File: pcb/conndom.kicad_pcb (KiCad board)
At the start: 2 copper layers, 0 parts

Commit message: first pcb design
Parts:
- added C1: 104, Capacitor_SMD:C_0805_2012Metric, F.Cu at (180.6, 92.7)
- added D1: SK6812, LED_SMD:LED_SK6812_PLCC4_5.0x5.0mm_P3.2mm, F.Cu at (183.4, 87.5)
- added J1: 5V, rpi-zero-2-w-testpads:2mm-testpad-conn-plated, F.Cu at (155.8, 103.7)
- added J10: USB A WIFI, UJ2-AH-4-TH:CUI_UJ2-AH-4-TH, F.Cu at (170.4, 105.4)
- added J2: GND, rpi-zero-2-w-testpads:2mm-testpad-conn-plated, F.Cu at (156.1, 106.3)
- added J3: USB_DP, rpi-zero-2-w-testpads:1.7mm-testpad-conn-plated, F.Cu at (142.3, 108.1)
- added J4: USB_DM, rpi-zero-2-w-testpads:1.7mm-testpad-conn-plated, F.Cu at (144.4, 108.1)
- added J5: 3V3, rpi-zero-2-w-testpads:2mm-testpad-conn-plated, F.Cu at (118.5, 87.5)
- added J6: GND, rpi-zero-2-w-testpads:2mm-testpad-conn-plated, F.Cu at (158.7, 84.8)
- added J7: PWR, rpi-zero-2-w-testpads:1.7mm-testpad-conn-plated, F.Cu at (158.7, 82.2)
- added J8: LED, rpi-zero-2-w-testpads:1.7mm-testpad-conn-plated, F.Cu at (156.1, 82.2)
- added J9: USB C PWR, UJC-HP2-3-SMT-TR:CUI_UJC-HP2-3-SMT-TR, F.Cu at (196.3, 87.4)
- added R1: 10k, Resistor_SMD:R_0805_2012Metric, F.Cu at (172.8, 93.0)
- added R2: 500, Resistor_SMD:R_0805_2012Metric, F.Cu at (178.6, 84.1)
- added R3: 5K1, Resistor_SMD:R_0805_2012Metric, F.Cu at (188.9, 82.9)
- added R4: 5K1, Resistor_SMD:R_0805_2012Metric, F.Cu at (187.8, 89.0)
- added REF**: zero-2-w-testpads, rpi-zero-2-w-testpads:rpi-zero-2-w-testpads, F.Cu at (167.0, 110.0)
- added S1: PWR, TS02-66-55-BK-260-LCR-D:SW_TS02-66-55-BK-260-LCR-D, F.Cu at (172.8, 87.4)
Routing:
- net GND: track 0.00 -> 123.7 mm, vias 0 -> 2
- net Net-(D1-VDD): track 0.00 -> 76.7 mm
- net +5V: track 0.00 -> 54.2 mm, vias 0 -> 2
- net Net-(J3-Pin_1): track 0.00 -> 31.1 mm
- net Net-(J4-Pin_1): track 0.00 -> 29.1 mm
- net Net-(J7-Pin_1): track 0.00 -> 27.4 mm, vias 0 -> 1
- net Net-(J8-Pin_1): track 0.00 -> 24.2 mm, vias 0 -> 1
- net Net-(J9-CC2): track 0.00 -> 6.05 mm
- net Net-(J9-CC1): track 0.00 -> 4.48 mm
- net Net-(D1-DIN): track 0.00 -> 3.26 mm
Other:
- board outline added: 82 x 32 mm

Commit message: fix missplaced pads for usb dp, dm
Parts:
- moved J3 2.15 mm to (144.4, 108.1)
- moved J4 2.15 mm to (142.3, 108.1)
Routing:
- net Net-(J4-Pin_1): track 29.1 -> 31.9 mm, vias 0 -> 1
- net Net-(J3-Pin_1): track 31.1 -> 29.0 mm
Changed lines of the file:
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@@
 	(footprint "rpi-zero-2-w-testpads:1.7mm-testpad-conn-plated"
 		(layer "F.Cu")
-		(at 142.3 108.1)
+		(at 144.45 108.1)
 		(property "Reference" "J3"
 			(at -15 6 0)
@@
 	(footprint "rpi-zero-2-w-testpads:1.7mm-testpad-conn-plated"
 		(layer "F.Cu")
-		(at 144.45 108.1)
+		(at 142.3 108.1)
 		(property "Reference" "J4"
 			(at -15 6 0)
@@
 	)
 	(segment
-		(start 149.5 100.9)
-		(end 142.3 108.1)
+		(start 150.75 101.8)
+		(end 168.7 101.8)
 		(width 0.5)
 		(layer "B.Cu")
@@
 	)
 	(segment
-		(start 170.43 100.9)
-		(end 149.5 100.9)
+		(start 144.45 108.1)
+		(end 150.75 101.8)
 		(width 0.5)
 		(layer "B.Cu")
@@
 	)
 	(segment
-		(start 166.9 102.9)
-		(end 165.75 101.75)
+		(start 169.6 100.9)
+		(end 170.43 100.9)
 		(width 0.5)
 		(layer "B.Cu")
-		(net 7)
+		(net 6)
 	)
 	(segment
-		(start 150.8 101.75)
-		(end 144.45 108.1)
+		(start 168.7 101.8)
+		(end 169.6 100.9)
 		(width 0.5)
 		(layer "B.Cu")
+		(net 6)
+	)
+	(segment
+		(start 169.7 102.9)
+		(end 170.43 102.9)
+		(width 0.5)
+		(layer "F.Cu")
+		(net 7)
+	)
+	(segment
+		(start 167.8 101)
+		(end 169.7 102.9)
+		(width 0.5)
+		(layer "F.Cu")
+		(net 7)
+	)
+	(via
+		(at 167.8 101)
+		(size 0.7)
+		(drill 0.3)
+		(layers "F.Cu" "B.Cu")
+		(free yes)
 		(net 7)
 	)
 	(segment
-		(start 170.43 102.9)
-		(end 166.9 102.9)
+		(start 149.4 101)
+		(end 167.8 101)
 		(width 0.5)
 		(layer "B.Cu")
@@
 	)
 	(segment
-		(start 165.75 101.75)
-		(end 150.8 101.75)
+		(start 142.3 108.1)
+		(end 149.4 101)
 		(width 0.5)
 		(layer "B.Cu")

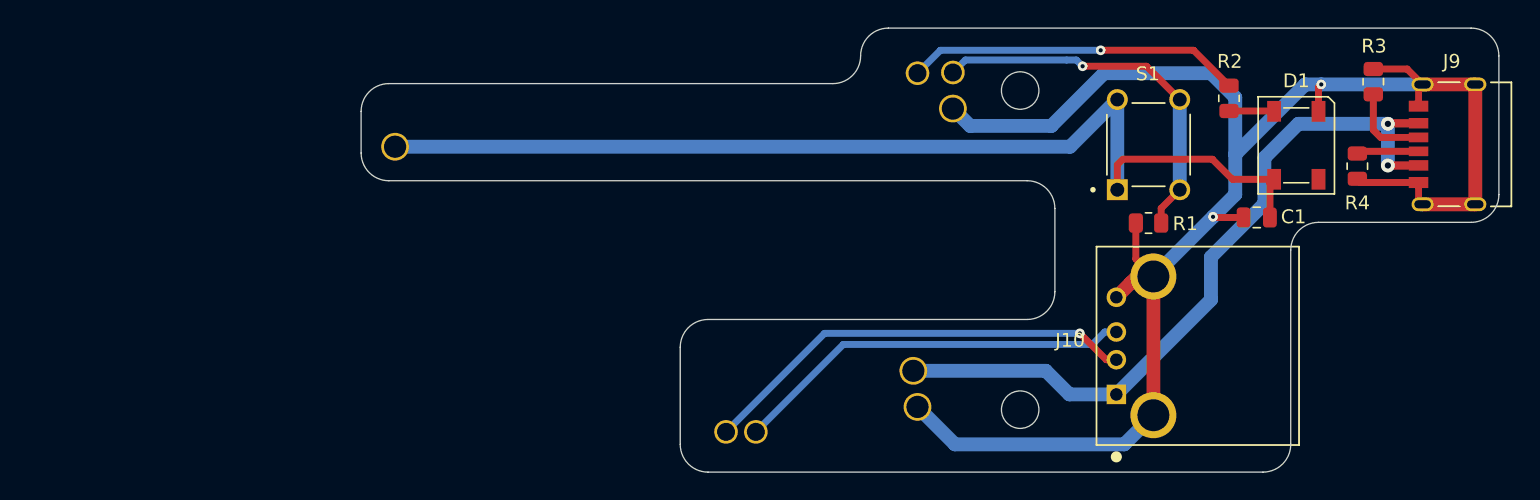
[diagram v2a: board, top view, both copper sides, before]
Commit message: update footprints, renaming
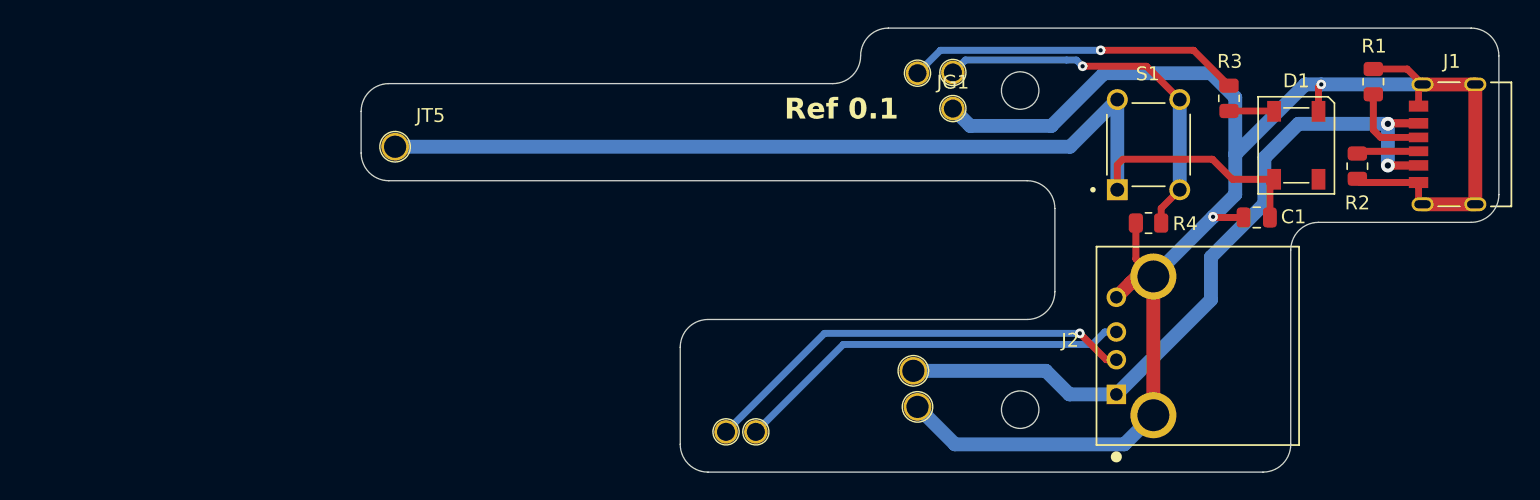
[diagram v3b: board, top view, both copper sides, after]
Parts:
- JG1: renamed from J6; footprint rpi-zero-2-w-testpads:2mm-testpad-conn-plated -> rpi-zero-2-w-testpads:1.7mm-testpad-conn-plated
- JG2: renamed from J7; value PWR -> GPIO21
- JG3: renamed from J8; value LED -> GPIO12
- renumbered J9 to J1, J10 to J2, J1 to JT1, J2 to JT2, J3 to JT3, J4 to JT4, J5 to JT5, R3 to R1, R4 to R2, R2 to R3, R1 to R4
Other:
- board text added: "Ref 0.1"

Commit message: pcb rev 0.2
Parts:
- moved JG3 17.6 mm to (138.5, 82.2)
- moved R4 16.2 mm to (161.3, 81.5), turned to 180 degrees
- moved R1 12.3 mm to (176.9, 85.1)
- moved R3 12.2 mm to (166.8, 87.0)
- moved J1 12.1 mm to (184.2, 87.0)
- moved D1 11.7 mm to (171.7, 87.0)
- moved S1 11.4 mm to (161.3, 87.0), turned to -90 degrees
- moved R2 10.9 mm to (176.9, 88.9)
- moved J2 10.9 mm to (159.6, 104.3)
- moved JG1 10.0 mm to (148.6, 84.8)
- moved JG2 10.0 mm to (148.6, 82.2)
- moved JT1 10.0 mm to (145.8, 103.7)
- moved JT3 10.0 mm to (134.4, 108.1)
- moved JT2 10.0 mm to (146.1, 106.3)
- moved JT5 10.0 mm to (108.5, 87.6)
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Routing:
- net GND: track 123.7 -> 108.9 mm
- net Net-(JG3-Pin_1): track 24.2 -> 34.0 mm
- net Net-(JG2-Pin_1): track 27.4 -> 21.2 mm, vias 1 -> 0
- net +5V: track 54.2 -> 48.0 mm
- net Net-(J1-CC2): track 6.05 -> 3.41 mm
- net Net-(D1-VDD): track 76.7 -> 74.1 mm
- net Net-(D1-DIN): track 3.26 -> 5.71 mm
- net Net-(J1-CC1): track 4.48 -> 3.41 mm
- net Net-(JT4-Pin_1): track 31.9 -> 31.0 mm
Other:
- board size 82 x 32 mm -> 91 x 30 mm
- board text added: "conndom Rev 0.2"
- board text removed: "Ref 0.1"
